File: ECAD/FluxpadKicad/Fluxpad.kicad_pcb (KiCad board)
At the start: 2 copper layers, 39 x 60 mm, 26 parts, among them SW1 SW_SPST, SW2 SW_SPST, SW3 PEC12R-4017F-N0024, U1 SeeeduinoXIAO, U2 DRV5056A3QDBZx Lekker, U3 DRV5056A3QDBZx Lekker

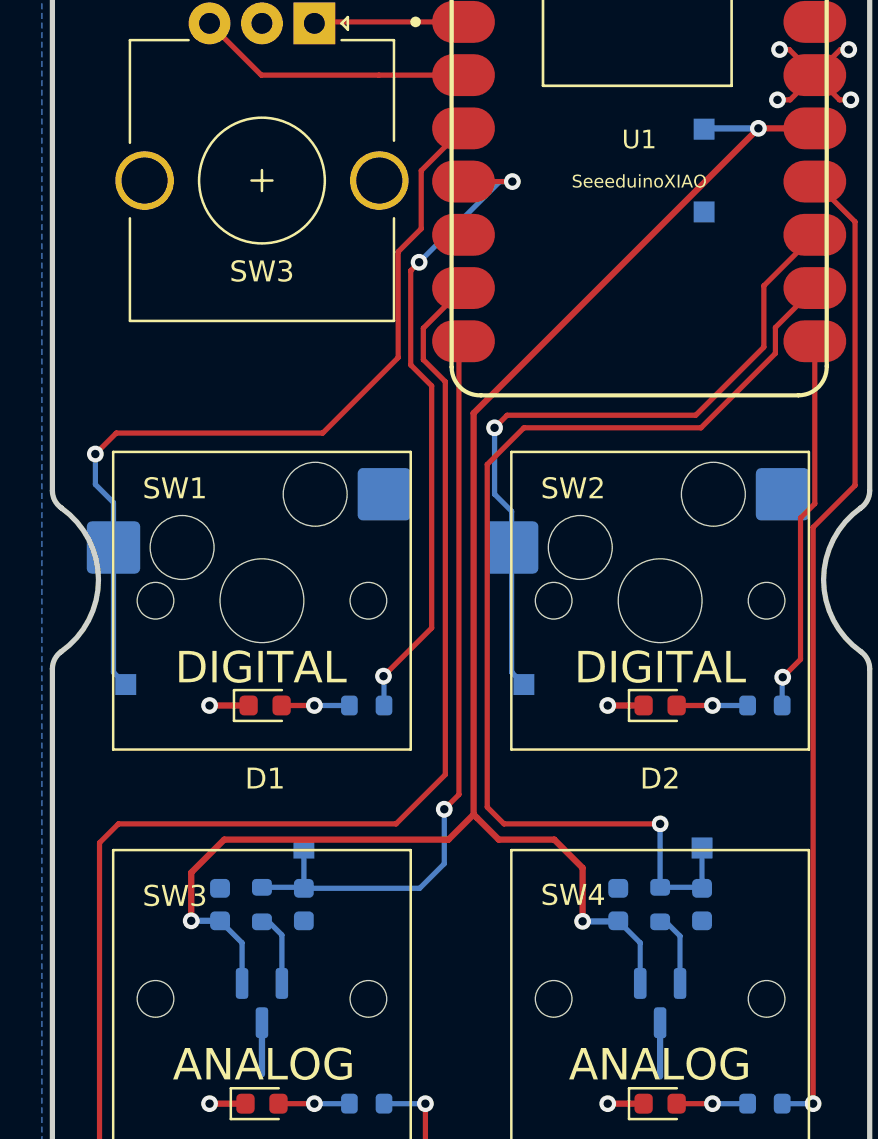
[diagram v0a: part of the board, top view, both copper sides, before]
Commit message: rename kicad project from tang to fluxpad
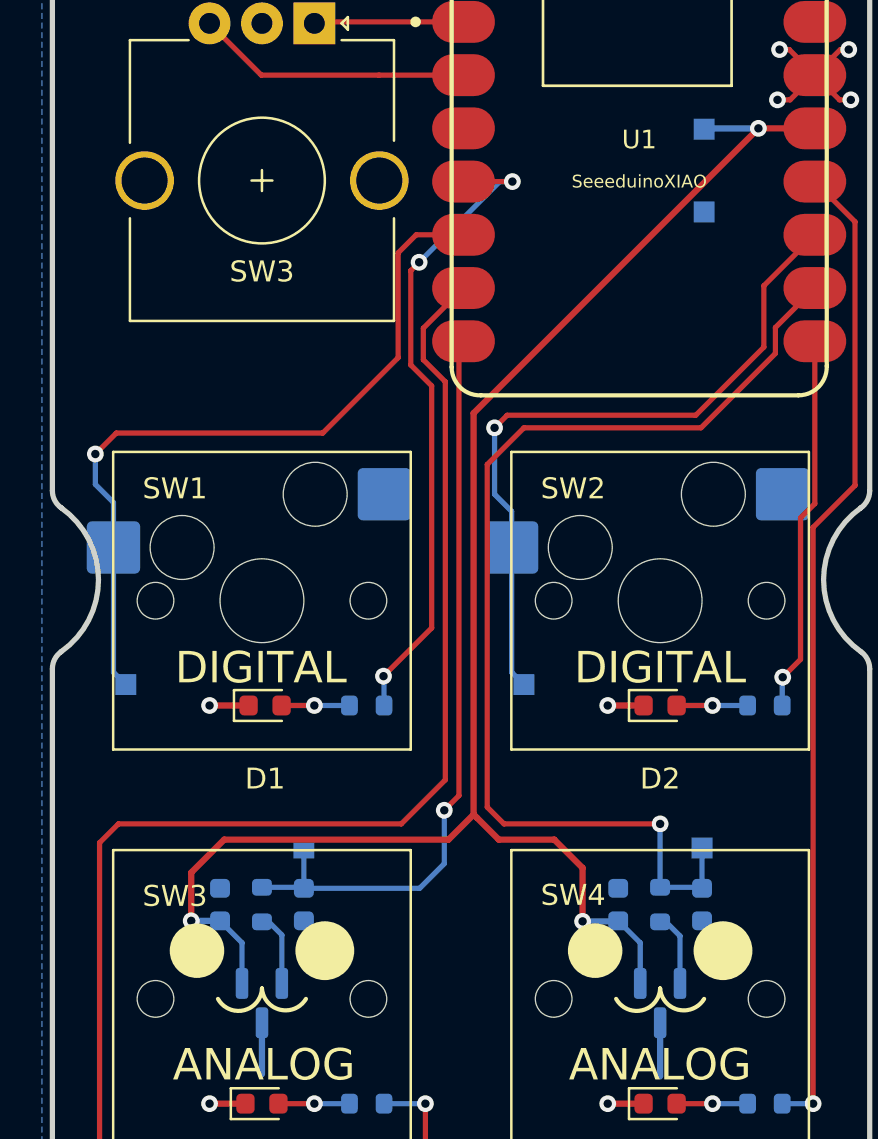
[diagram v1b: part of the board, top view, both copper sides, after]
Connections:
- U1 pad 3: SW1 -> unconnected-(U1-Pad3)
- U1 pad 5: unconnected-(U1-Pad5) -> SW1
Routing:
- net SW1: track 40.2 -> 36.4 mm
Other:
- board text added: "FLUXPAD Rev3 T.W."
- board text removed: "FluxPad Rev 2 TW"

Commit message: initial commit for fluxpad 2
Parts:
- removed C3, C4: DNP, Capacitor_SMD:C_0603_1608Metric
- added 1V1: TestPoint, TestPoint:TestPoint_Pad_1.0x1.0mm, B.Cu at (157.2, 82.5)
- added C11: 100n, Capacitor_SMD:C_0402_1005Metric, B.Cu at (166.3, 85.9)
- added C12: 100n, Capacitor_SMD:C_0402_1005Metric, B.Cu at (165.7, 96.3)
- added C14: 100n, Capacitor_SMD:C_0402_1005Metric, B.Cu at (170.4, 92.2)
- added C15: 100n, Capacitor_SMD:C_0402_1005Metric, B.Cu at (170.4, 93.3)
- added C16: 100n, Capacitor_SMD:C_0402_1005Metric, B.Cu at (158.5, 92.0)
- added C17: 1u, Capacitor_SMD:C_0402_1005Metric, B.Cu at (159.8, 86.5)
- added C18: 1u, Capacitor_SMD:C_0402_1005Metric, B.Cu at (150.7, 93.7)
- added C19: 100n, Capacitor_SMD:C_0402_1005Metric, B.Cu at (158.5, 93.1)
- added C20: 30p, Capacitor_SMD:C_0402_1005Metric, B.Cu at (170.3, 90.0)
- added C21: 30p, Capacitor_SMD:C_0402_1005Metric, B.Cu at (173.6, 86.9)
- added C22: 1uF, Capacitor_SMD:C_0402_1005Metric, B.Cu at (177.5, 125.5)
- added C5: 22uf, Capacitor_SMD:C_0805_2012Metric, B.Cu at (149.3, 97.9)
- added C6: 10uf, Capacitor_SMD:C_0603_1608Metric, B.Cu at (131.9, 93.8)
- added C7: 100n, Capacitor_SMD:C_0402_1005Metric, B.Cu at (160.9, 96.3)
- added C8: 100n, Capacitor_SMD:C_0402_1005Metric, B.Cu at (162.2, 85.9)
- added C9: 100n, Capacitor_SMD:C_0402_1005Metric, B.Cu at (162.0, 96.3)
- added D5: WS2812B, LED_SMD:LED_WS2812B_PLCC4_5.0x5.0mm_P3.2mm, F.Cu at (162.0, 93.5)
- added D6: WS2812B, LED_SMD:LED_WS2812B_PLCC4_5.0x5.0mm_P3.2mm, F.Cu at (171.0, 93.5)
- added D7: WS2812B, LED_SMD:LED_WS2812B_PLCC4_5.0x5.0mm_P3.2mm, F.Cu at (180.0, 93.5)
- added D8: WHITE LED, LED_SMD:LED_0603_1608Metric, F.Cu at (179.0, 134.0)
- added H1: MountingHole, MountingHole:MountingHole_2.2mm_M2_ISO7380, F.Cu at (128.0, 104.5)
- added H2: MountingHole, MountingHole:MountingHole_2.2mm_M2_ISO7380, F.Cu at (142.0, 143.5)
- added H3: MountingHole, MountingHole:MountingHole_2.2mm_M2_ISO7380, F.Cu at (178.0, 143.5)
- added H4: MountingHole, MountingHole:MountingHole_2.2mm_M2_ISO7380, F.Cu at (192.0, 104.5)
- added H5: MountingHole, MountingHole:MountingHole_2.2mm_M2_ISO7380, F.Cu at (154.0, 98.0)
- added H6: Tooling Hole, Tang:JLC Tooling Hole, F.Cu at (148.7, 89.3)
- added H7: Tooling Hole, Tang:JLC Tooling Hole, F.Cu at (133.4, 138.2)
- added H8: Tooling Hole, Tang:JLC Tooling Hole, F.Cu at (187.2, 137.3)
- added J1: USB_C_Receptacle_USB2.0, Tang:USB_C_Receptacle_HRO_TYPE-C-31-M-12, B.Cu at (138.0, 91.2)
- added J4: DEBUG, Connector_PinHeader_1.27mm:PinHeader_1x05_P1.27mm_Vertical, F.Cu at (167.2, 81.1)
- added R10: 10k, Resistor_SMD:R_0402_1005Metric, B.Cu at (178.0, 86.8)
- added R11: 22, Resistor_SMD:R_0402_1005Metric, B.Cu at (158.4, 95.4)
- added R12: 22, Resistor_SMD:R_0402_1005Metric, B.Cu at (159.5, 95.4)
- added R13: 1k, Resistor_SMD:R_0402_1005Metric, B.Cu at (178.0, 87.9)
- added R14: 820R, Resistor_SMD:R_0402_1005Metric, B.Cu at (160.8, 121.5)
- added R15: 22, Resistor_SMD:R_0603_1608Metric, B.Cu at (183.6, 134.0)
- added R16: 820R, Resistor_SMD:R_0402_1005Metric, B.Cu at (160.8, 117.7)
- added R17: 5.6K, Resistor_SMD:R_0402_1005Metric, B.Cu at (163.0, 117.7)
- added R18: 10K, Resistor_SMD:R_0402_1005Metric, B.Cu at (164.1, 117.7)
- added R19: 220R, Resistor_SMD:R_0402_1005Metric, B.Cu at (177.1, 120.7)
- added R20: 820R, Resistor_SMD:R_0402_1005Metric, B.Cu at (178.2, 120.7)
- added R21: 5.6K, Resistor_SMD:R_0402_1005Metric, B.Cu at (163.0, 121.5)
- added R22: 5.6K, Resistor_SMD:R_0402_1005Metric, B.Cu at (176.0, 120.7)
- added R23: 10K, Resistor_SMD:R_0402_1005Metric, B.Cu at (164.1, 121.5)
- added R24: 10K, Resistor_SMD:R_0402_1005Metric, B.Cu at (174.9, 120.7)
- added R7: 5.1k, Resistor_SMD:R_0402_1005Metric, B.Cu at (132.2, 91.0)
- added R8: 5.1k, Resistor_SMD:R_0402_1005Metric, B.Cu at (143.8, 91.0)
- added R9: 10k, Resistor_SMD:R_0402_1005Metric, B.Cu at (170.1, 96.6)
- added SW4: RESET, Tang:SPST SMD TS-1187A-B-A-B, B.Cu at (182.9, 94.6)
- added SW5: BOOTSEL, Tang:SPST SMD TS-1187A-B-A-B, B.Cu at (182.9, 88.5)
- added SW6: SW_SPST, Tang:Kailh Hot Swap Socket, B.Cu at (159.4, 106.2)
- added SW7: SW_SPST, Tang:Kailh Hot Swap Socket, B.Cu at (178.4, 106.2)
- added U4: RP2040, Package_DFN_QFN:QFN-56-1EP_7x7mm_P0.4mm_EP3.2x3.2mm, B.Cu at (164.7, 91.0)
- added U5: DRV5056A3QDBZx Lekker, Tang:SW_Cherry_MX_PCB_1.00u_hall_effect, B.Cu at (179.0, 129.0)
- added U6: W25Q128JVS, Tang:SOIC-8_5.23x5.23mm_P1.27mm, B.Cu at (154.3, 90.6)
- added U7: USBLC6-2SC6, Package_TO_SOT_SMD:SOT-23-6, B.Cu at (143.8, 101.6)
- added U8: AMS1117-3.3, Package_TO_SOT_SMD:SOT-223-3_TabPin2, B.Cu at (136.0, 103.5)
- added Y1: Crystal_GND24, Crystal:Crystal_SMD_3225-4Pin_3.2x2.5mm, B.Cu at (172.0, 88.5)
- C1, C2: value 0.1uF -> 1uF; footprint Capacitor_SMD:C_0603_1608Metric -> Capacitor_SMD:C_0402_1005Metric
- D1, D2, D3, D4: value LED -> WHITE LED
- R1, R2, R3, R4: value 20 -> 22
- R5, R6: value 0 -> 220R; footprint Resistor_SMD:R_0603_1608Metric -> Resistor_SMD:R_0402_1005Metric
- SW1, SW2: footprint Switch_Keyboard_Hotswap_Kailh:SW_Hotswap_Kailh_MX_1.00u -> Tang:SW_Hotswap_Kailh_MX_no_pads
- U1: value SeeeduinoXIAO -> LM324A; footprint Tang:Seeeduino XIAO-MOUDLE14P-2.54-21X17.8MM -> Package_SO:SOIC-14_3.9x8.7mm_P1.27mm; moved to B.Cu
- moved U1 59.9 mm to (169.5, 119.7), turned to 180 degrees
- moved SW3 55.3 mm to (138.5, 117.5), turned to 90 degrees
- moved TP_SW3 53.9 mm to (166.0, 114.1)
- moved R5 51.9 mm to (161.9, 117.7)
- moved D1 51.4 mm to (160.2, 115.0)
- moved D2 51.4 mm to (179.0, 115.0)
- moved SW1 51.4 mm to (160.0, 110.0)
- moved SW2 51.4 mm to (179.0, 110.0)
- moved TP_SW2 50.1 mm to (173.1, 101.9)
- moved R1 49.2 mm to (162.9, 114.2), turned to 90 degrees
- moved R2 49.0 mm to (181.7, 114.2), turned to 90 degrees
- moved TP_SW1 47.9 mm to (150.7, 110.7)
- moved 3V3 46.8 mm to (177.7, 81.3)
- moved TP_SW4 36.0 mm to (163.7, 123.9)
- moved C1 34.8 mm to (140.1, 125.0)
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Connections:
- C1 pad 1: +3V3 -> +5V
- C2 pad 1: +3V3 -> +5V
- R1 pad 2: LED1 -> /LED1
- R2 pad 2: LED2 -> /LED2
- R3 pad 2: LED3 -> /LED3
- R4 pad 2: LED4 -> /LED4
- R5 pad 1: Net-(R5-Pad1) -> +5V
- R5 pad 2: SW3 -> Net-(R16-Pad2)
- R6 pad 1: Net-(R6-Pad1) -> +5V
- R6 pad 2: SW4 -> Net-(R14-Pad2)
- SW3 pad A: ENCA -> /ENCA
- SW3 pad B: ENCB -> /ENCB
- U1 pad 1: ENCA -> unconnected-(U1-Pad1)
- U1 pad 10: SW2 -> Net-(U1C-+)
- U1 pad 11: LED4 -> GND
- U1 pad 12: +3V3 -> Net-(U1D-+)
- U1 pad 13: GND -> Net-(U1D--)
- U1 pad 14: +5V -> SW3
- U1 pad 2: ENCB -> unconnected-(U1A---Pad2)
- U1 pad 4: LED1 -> +5V
- U1 pad 5: SW1 -> Net-(U1B-+)
- U1 pad 6: LED3 -> Net-(U1B--)
- U1 pad 7: SW3 -> /SW5
- U1 pad 8: LED2 -> SW4
- U1 pad 9: SW4 -> Net-(U1C--)
- U2 pad 1: +3V3 -> +5V
- U2 pad 2: Net-(R5-Pad1) -> Net-(U1D-+)
- U3 pad 1: +3V3 -> +5V
- U3 pad 2: Net-(R6-Pad1) -> Net-(U1C-+)
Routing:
- net +5V: track 0.00 -> 188.1 mm, vias 0 -> 15
- net GND: track 20.4 -> 113.4 mm, vias 8 -> 66
- net LED3: track 77.2 -> 0.00 mm, vias 1 -> 0
- net /LED5: track 0.00 -> 75.3 mm, vias 0 -> 2
- net /LED4: track 0.00 -> 67.4 mm, vias 0 -> 2
- net /LED1: track 0.00 -> 64.3 mm, vias 0 -> 2
- net /LED3: track 0.00 -> 63.0 mm, vias 0 -> 2
- net /LED2: track 0.00 -> 54.9 mm, vias 0 -> 2
- net LED4: track 47.0 -> 0.00 mm, vias 1 -> 0
- net /ENCA: track 0.00 -> 42.3 mm, vias 0 -> 3
- net /SW5: track 0.00 -> 38.9 mm, vias 0 -> 2
- net /ENCB: track 0.00 -> 38.7 mm, vias 0 -> 3
- net /QSPI_SS: track 0.00 -> 32.8 mm
- net LED1: track 31.1 -> 0.00 mm, vias 3 -> 0
- net Net-(U1D-+): track 0.00 -> 30.7 mm
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- added copper zone on In1.Cu, net +3V3
- added copper zone on In1.Cu, net +5V
- added copper zone on F.Cu, net GND
- added copper zone on In2.Cu, net GND
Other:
- board size 39 x 60 mm -> 70 x 68 mm
- copper layers 2 -> 4
- board text added: "FLUXPAD RevA T.W."
- board text removed: "FLUXPAD Rev3 T.W."

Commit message: kicad changes
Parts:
- removed 1V1, TP_SW1, TP_SW2, TP_SW3, TP_SW4: TestPoint, TestPoint:TestPoint_Pad_1.0x1.0mm
- removed J4: DEBUG, Connector_PinHeader_1.27mm:PinHeader_1x05_P1.27mm_Vertical
- removed R17, R21, R22: 5.6K, Resistor_SMD:R_0402_1005Metric
- removed R18, R23, R24: 10K, Resistor_SMD:R_0402_1005Metric
- removed R19: 220R, Resistor_SMD:R_0402_1005Metric
- removed R20: 820R, Resistor_SMD:R_0402_1005Metric
- added C10: 1uF, Capacitor_SMD:C_0402_1005Metric, F.Cu at (184.4, 94.0)
- added C13: 100n, Capacitor_SMD:C_0402_1005Metric, B.Cu at (158.5, 93.3)
- added C23: 1uF, Capacitor_SMD:C_0402_1005Metric, B.Cu at (160.2, 125.0)
- added C24: 1uF, Capacitor_SMD:C_0402_1005Metric, B.Cu at (141.2, 125.0)
- added C25: 1uF, Capacitor_SMD:C_0402_1005Metric, B.Cu at (179.2, 125.0)
- added C3: 1uF, Capacitor_SMD:C_0402_1005Metric, F.Cu at (166.5, 94.0)
- added C4: 1uF, Capacitor_SMD:C_0402_1005Metric, F.Cu at (175.4, 94.0)
- added G***: LOGO, assets:lines_logo, F.Cu at (158.9, 130.5)
- added G***: LOGO, assets:pippi, B.Cu at (191.3, 138.3)
- D1, D2, D3, D4: footprint LED_SMD:LED_0603_1608Metric -> Tang:1208 Counterpost LED; moved to B.Cu
- D5: renamed from D8; footprint LED_SMD:LED_0603_1608Metric -> Tang:1208 Counterpost LED; moved to B.Cu
- R14, R16: value 820R -> 100; footprint Resistor_SMD:R_0402_1005Metric -> Resistor_SMD:R_0603_1608Metric
- R5: value 220R -> 560; footprint Resistor_SMD:R_0402_1005Metric -> Resistor_SMD:R_0603_1608Metric; moved to F.Cu
- R6: value 220R -> 100; footprint Resistor_SMD:R_0402_1005Metric -> Resistor_SMD:R_0603_1608Metric
- SW3: value PEC12R-4017F-N0024 -> EC12E24204A7
- U1: value LM324A -> 74AHCT1G125; footprint Package_SO:SOIC-14_3.9x8.7mm_P1.27mm -> Package_TO_SOT_SMD:SOT-353_SC-70-5; moved to F.Cu
- moved 3V3 55.1 mm to (130.4, 109.6)
- moved GND1 45.8 mm to (130.4, 114.2)
- moved U1 29.2 mm to (156.5, 93.5), turned to 0 degrees
- moved R5 22.7 mm to (156.5, 95.7), turned to 0 degrees
- moved R16 20.8 mm to (180.3, 125.0)
- moved R6 19.9 mm to (142.3, 125.0), turned to 90 degrees
- moved R14 3.54 mm to (161.3, 125.0), turned to 90 degrees
- moved R2 2.44 mm to (184.0, 115.0), turned to 0 degrees
- moved R1 2.44 mm to (165.2, 115.0), turned to 0 degrees
- moved R9 2.22 mm to (170.4, 94.4), turned to 180 degrees
- moved C17 1.43 mm to (161.1, 85.9)
- moved C16 0.90 mm to (158.5, 91.1)
- moved C19 0.90 mm to (158.5, 92.2)
- moved C22 0.77 mm to (178.1, 125.0), turned to 90 degrees
- moved R15 0.40 mm to (184.0, 134.0)
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- renumbered D5 to D6, D6 to D7, D7 to D8
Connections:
- net SW1 renamed /SW1
- net SW2 renamed /SW2
- C1 pad 1: +5V -> +3V3
- C2 pad 1: +5V -> +3V3
- C22 pad 1: +5V -> +3V3
- D6 pad 4: unconnected-(D5-DIN-Pad4) -> Net-(D6-DIN)
- D8 pad 2: /RGB_DOUT -> unconnected-(D8-DOUT-Pad2)
- R14 pad 1: GND -> Net-(U3-OUT)
- R14 pad 2: Net-(R14-Pad2) -> /SW4
- R16 pad 1: GND -> Net-(U5-OUT)
- R16 pad 2: Net-(R16-Pad2) -> /SW5
- R5 pad 1: +5V -> Net-(R5-Pad1)
- R5 pad 2: Net-(R16-Pad2) -> Net-(D6-DIN)
- R6 pad 1: +5V -> Net-(U2-OUT)
- R6 pad 2: Net-(R14-Pad2) -> /SW3
- U1 pad 1: unconnected-(U1-Pad1) -> GND
- U1 pad 2: unconnected-(U1A---Pad2) -> /RGB_DOUT
- U1 pad 3: unconnected-(U1A-+-Pad3) -> GND
- U1 pad 4: +5V -> Net-(R5-Pad1)
- U1 pad 5: Net-(U1B-+) -> +5V
- U2 pad 1: +5V -> +3V3
- U2 pad 2: Net-(U1D-+) -> Net-(U2-OUT)
- U3 pad 1: +5V -> +3V3
- U3 pad 2: Net-(U1C-+) -> Net-(U3-OUT)
- U4 pad 39: SW4 -> /SW4
- U4 pad 40: SW3 -> /SW3
- U5 pad 1: +5V -> +3V3
- U5 pad 2: Net-(U1B-+) -> Net-(U5-OUT)
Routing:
- net +5V: track 188.1 -> 107.7 mm, vias 15 -> 8
- net /SW3: track 0.00 -> 54.4 mm
- net SW4: track 40.2 -> 0.00 mm, vias 2 -> 0
- net /SW4: track 0.00 -> 36.7 mm
- net Net-(U1D-+): track 30.7 -> 0.00 mm
- net SW3: track 29.6 -> 0.00 mm
- net Net-(U1B-+): track 18.7 -> 0.00 mm
- net GND: track 113.4 -> 97.5 mm, vias 66 -> 51
- net Net-(U1C-+): track 15.7 -> 0.00 mm
- net /SWCLK: track 15.2 -> 0.00 mm, vias 3 -> 0
- net /SWDIO: track 14.9 -> 0.00 mm, vias 3 -> 0
- net /UART0_RX: track 12.0 -> 0.00 mm, vias 1 -> 0
- net /UART0_TX: track 11.2 -> 0.00 mm, vias 1 -> 0
- net +1V1: track 27.9 -> 21.0 mm, vias 6 -> 4
- net +3V3: track 53.2 -> 59.6 mm
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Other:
- board text added: "FLUXPAD"
- board text added: "FLUXPAD V2 RevB T.W."
- board text removed: "FLUXPAD RevA T.W."
